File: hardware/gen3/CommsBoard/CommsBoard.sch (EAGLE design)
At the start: 41 parts, among them U1 ATMEGA165PV-8AU

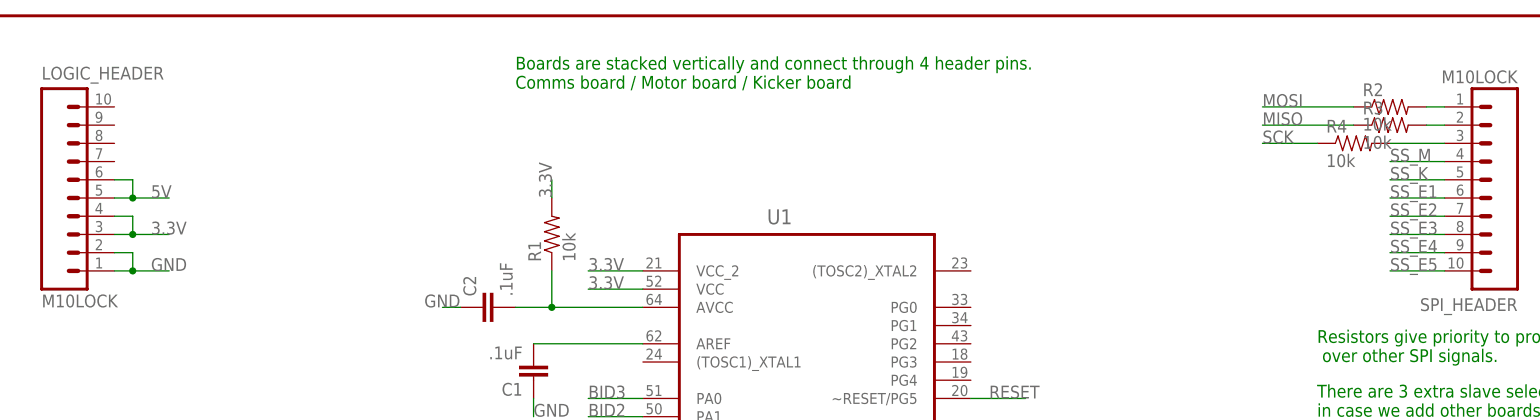
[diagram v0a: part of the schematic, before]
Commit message: some decoupling for power lines
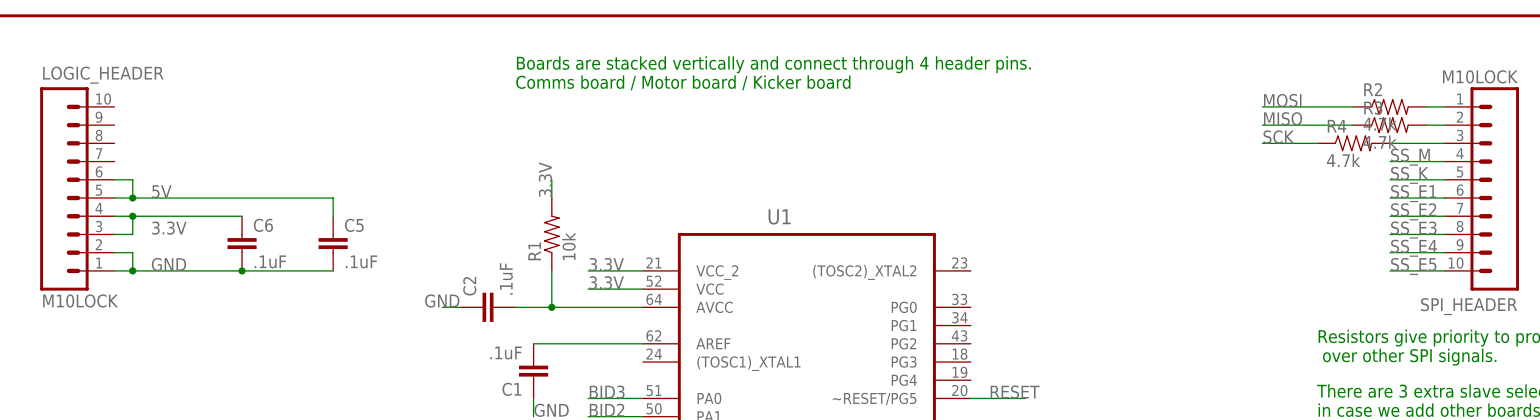
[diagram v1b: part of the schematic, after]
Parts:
- added C5, C6: .1uF, SparkFun-Capacitors:CAP0805
- R2, R3, R4: value 10k -> 4.7k
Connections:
- net 3.3V: now also C6.1
- net 5V: now also C5.1
- net GND: now also C5.2, C6.2
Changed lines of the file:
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@@
 <layers>
 <layer number="1" name="Top" color="4" fill="1" visible="no" active="no"/>
+<layer number="2" name="Route2" color="1" fill="3" visible="no" active="no"/>
+<layer number="3" name="Route3" color="4" fill="3" visible="no" active="no"/>
+<layer number="14" name="Route14" color="1" fill="6" visible="no" active="no"/>
+<layer number="15" name="Route15" color="4" fill="6" visible="no" active="no"/>
 <layer number="16" name="Bottom" color="1" fill="1" visible="no" active="no"/>
 <layer number="17" name="Pads" color="2" fill="1" visible="no" active="no"/>
@@
 <layer number="223" name="223bmp" color="24" fill="1" visible="no" active="no"/>
 <layer number="224" name="224bmp" color="25" fill="1" visible="no" active="no"/>
+<layer number="225" name="225bmp" color="7" fill="1" visible="yes" active="yes"/>
+<layer number="226" name="226bmp" color="7" fill="1" visible="yes" active="yes"/>
+<layer number="227" name="227bmp" color="7" fill="1" visible="yes" active="yes"/>
+<layer number="228" name="228bmp" color="7" fill="1" visible="yes" active="yes"/>
+<layer number="229" name="229bmp" color="7" fill="1" visible="yes" active="yes"/>
+<layer number="230" name="230bmp" color="7" fill="1" visible="yes" active="yes"/>
+<layer number="231" name="231bmp" color="7" fill="1" visible="yes" active="yes"/>
 <layer number="248" name="Housing" color="7" fill="1" visible="yes" active="yes"/>
 <layer number="249" name="Edge" color="7" fill="1" visible="yes" active="yes"/>
@@
 <part name="C2" library="SparkFun-Capacitors" deviceset="CAP" device="0805" value=".1uF"/>
 <part name="R1" library="SparkFun-Passives" deviceset="RESISTOR" device="0805-RES" value="10k"/>
-<part name="R2" library="SparkFun-Passives" deviceset="RESISTOR" device="0805-RES" value="10k"/>
-<part name="R3" library="SparkFun-Passives" deviceset="RESISTOR" device="0805-RES" value="10k"/>
-<part name="R4" library="SparkFun-Passives" deviceset="RESISTOR" device="0805-RES" value="10k"/>
+<part name="R2" library="SparkFun-Passives" deviceset="RESISTOR" device="0805-RES" value="4.7k"/>
+<part name="R3" library="SparkFun-Passives" deviceset="RESISTOR" device="0805-RES" value="4.7k"/>
+<part name="R4" library="SparkFun-Passives" deviceset="RESISTOR" device="0805-RES" value="4.7k"/>
 <part name="FRAME2" library="SparkFun-Aesthetics" deviceset="FRAME-LETTER" device=""/>
 <part name="ROBID" library="SparkFun-Electromechanical" deviceset="4-POS-DIP" device=""/>
@@
 <part name="U1" library="gen3" deviceset="ATMEGA165PV-8AU" device=""/>
 <part name="JP1" library="SparkFun-Connectors" deviceset="M05X2" device="PTH"/>
+<part name="C5" library="SparkFun-Capacitors" deviceset="CAP" device="0805" value=".1uF"/>
+<part name="C6" library="SparkFun-Capacitors" deviceset="CAP" device="0805" value=".1uF"/>
 </parts>
 <sheets>
@@
 <instance part="U1" gate="A" x="129.54" y="106.68"/>
 <instance part="JP1" gate="G$1" x="76.2" y="38.1"/>
+<instance part="C5" gate="G$1" x="63.5" y="152.4"/>
+<instance part="C6" gate="G$1" x="50.8" y="152.4"/>
 </instances>
 <busses>
@@
 <label x="38.1" y="149.86" size="1.778" layer="95"/>
 <pinref part="LOGIC_HEADER" gate="G$1" pin="2"/>
-<wire x1="35.56" y1="149.86" x2="40.64" y2="149.86" width="0.1524" layer="91"/>
 <wire x1="33.02" y1="152.4" x2="35.56" y2="152.4" width="0.1524" layer="91"/>
 <wire x1="35.56" y1="152.4" x2="35.56" y2="149.86" width="0.1524" layer="91"/>
@@
 <wire x1="35.56" y1="149.86" x2="33.02" y2="149.86" width="0.1524" layer="91"/>
 <junction x="35.56" y="149.86"/>
+<pinref part="C6" gate="G$1" pin="2"/>
+<wire x1="35.56" y1="149.86" x2="50.8" y2="149.86" width="0.1524" layer="91"/>
+<pinref part="C5" gate="G$1" pin="2"/>
+<wire x1="50.8" y1="149.86" x2="63.5" y2="149.86" width="0.1524" layer="91"/>
+<junction x="50.8" y="149.86"/>
 </segment>
 <segment>
@@
 <label x="38.1" y="154.94" size="1.778" layer="95"/>
 <pinref part="LOGIC_HEADER" gate="G$1" pin="4"/>
-<wire x1="35.56" y1="154.94" x2="40.64" y2="154.94" width="0.1524" layer="91"/>
 <wire x1="33.02" y1="157.48" x2="35.56" y2="157.48" width="0.1524" layer="91"/>
 <wire x1="35.56" y1="157.48" x2="35.56" y2="154.94" width="0.1524" layer="91"/>
-<junction x="35.56" y="154.94"/>
+<pinref part="C6" gate="G$1" pin="1"/>
+<wire x1="35.56" y1="157.48" x2="50.8" y2="157.48" width="0.1524" layer="91"/>
+<junction x="35.56" y="157.48"/>
 </segment>
 <segment>
@@
 <label x="38.1" y="160.02" size="1.778" layer="95"/>
 <pinref part="LOGIC_HEADER" gate="G$1" pin="6"/>
-<wire x1="35.56" y1="160.02" x2="40.64" y2="160.02" width="0.1524" layer="91"/>
 <wire x1="33.02" y1="162.56" x2="35.56" y2="162.56" width="0.1524" layer="91"/>
 <wire x1="35.56" y1="162.56" x2="35.56" y2="160.02" width="0.1524" layer="91"/>
 <junction x="35.56" y="160.02"/>
-</segment>
-</net>
+<pinref part="C5" gate="G$1" pin="1"/>
+<wire x1="35.56" y1="160.02" x2="63.5" y2="160.02" width="0.1524" layer="91"/>
+<wire x1="63.5" y1="160.02" x2="63.5" y2="157.48" width="0.1524" layer="91"/>
+</segment>
+</net>

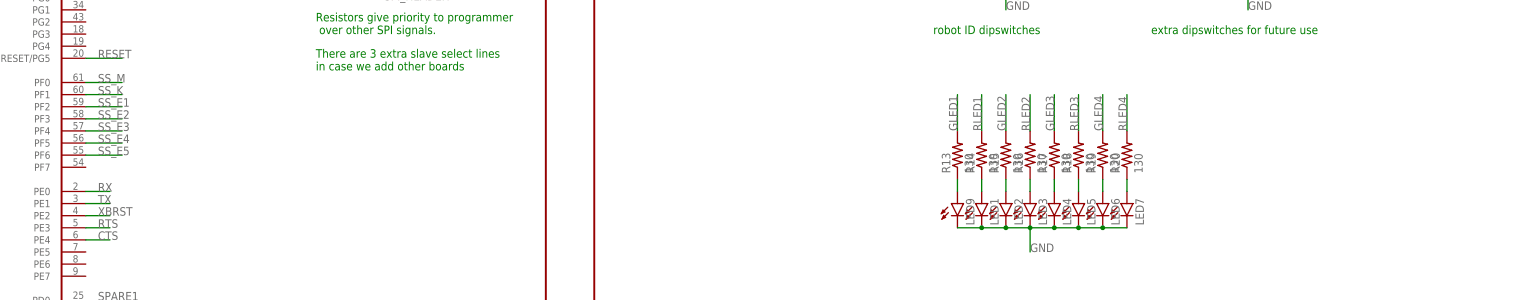
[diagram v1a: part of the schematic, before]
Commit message: added tmp sensor
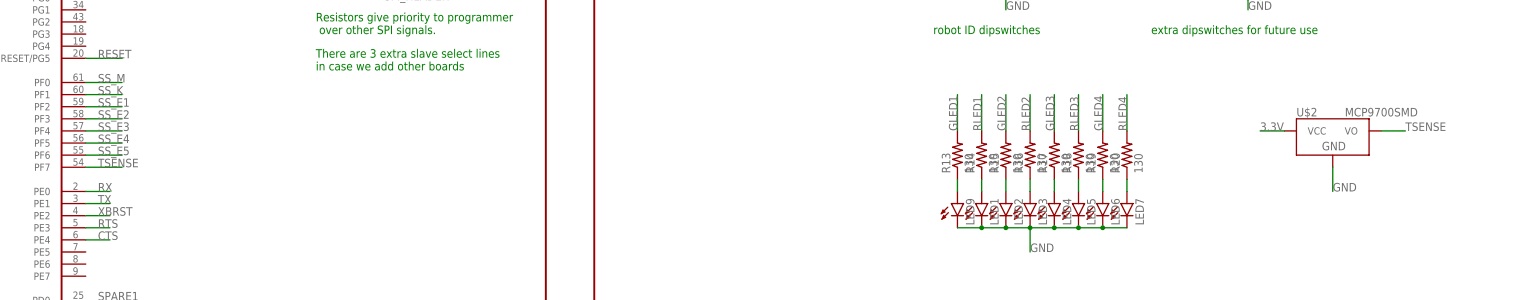
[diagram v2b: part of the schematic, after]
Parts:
- added U$2: MCP9700SMD, SparkFun-Sensors:MCP9700SMD
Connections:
- new net TSENSE: U$2.VO, U1.PF7
- net 3.3V: now also U$2.VCC
- net GND: now also U$2.GND
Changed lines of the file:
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@@
 <part name="C5" library="SparkFun-Capacitors" deviceset="CAP" device="0805" value=".1uF"/>
 <part name="C6" library="SparkFun-Capacitors" deviceset="CAP" device="0805" value=".1uF"/>
+<part name="U$2" library="SparkFun-Sensors" deviceset="MCP9700" device="SMD"/>
 </parts>
 <sheets>
@@
 <instance part="C5" gate="G$1" x="63.5" y="152.4"/>
 <instance part="C6" gate="G$1" x="50.8" y="152.4"/>
+<instance part="U$2" gate="G$1" x="414.02" y="114.3"/>
 </instances>
 <busses>
@@
 <label x="86.36" y="33.02" size="1.778" layer="95"/>
 </segment>
+<segment>
+<pinref part="U$2" gate="G$1" pin="GND"/>
+<wire x1="414.02" y1="109.22" x2="414.02" y2="104.14" width="0.1524" layer="91"/>
+<label x="414.02" y="104.14" size="1.778" layer="95"/>
+</segment>
 </net>
 <net name="3.3V" class="0">
@@
 <wire x1="83.82" y1="43.18" x2="88.9" y2="43.18" width="0.1524" layer="91"/>
 <label x="86.36" y="43.18" size="1.778" layer="95"/>
+</segment>
+<segment>
+<pinref part="U$2" gate="G$1" pin="VCC"/>
+<wire x1="403.86" y1="116.84" x2="398.78" y2="116.84" width="0.1524" layer="91"/>
+<label x="398.78" y="116.84" size="1.778" layer="95"/>
 </segment>
 </net>
@@
 </segment>
 </net>
+<net name="TSENSE" class="0">
+<segment>
+<pinref part="U$2" gate="G$1" pin="VO"/>
+<wire x1="424.18" y1="116.84" x2="429.26" y2="116.84" width="0.1524" layer="91"/>
+<label x="429.26" y="116.84" size="1.778" layer="95"/>
+</segment>
+<segment>
+<pinref part="U1" gate="A" pin="PF7"/>
+<wire x1="152.4" y1="109.22" x2="160.02" y2="109.22" width="0.1524" layer="91"/>
+<label x="154.94" y="109.22" size="1.778" layer="95"/>
+</segment>
+</net>

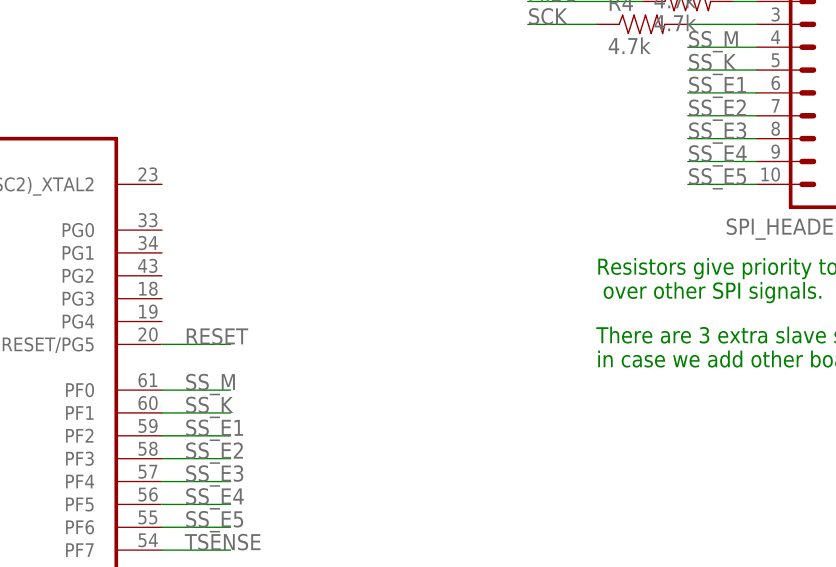
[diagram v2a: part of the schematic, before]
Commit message: Added reset button to comms
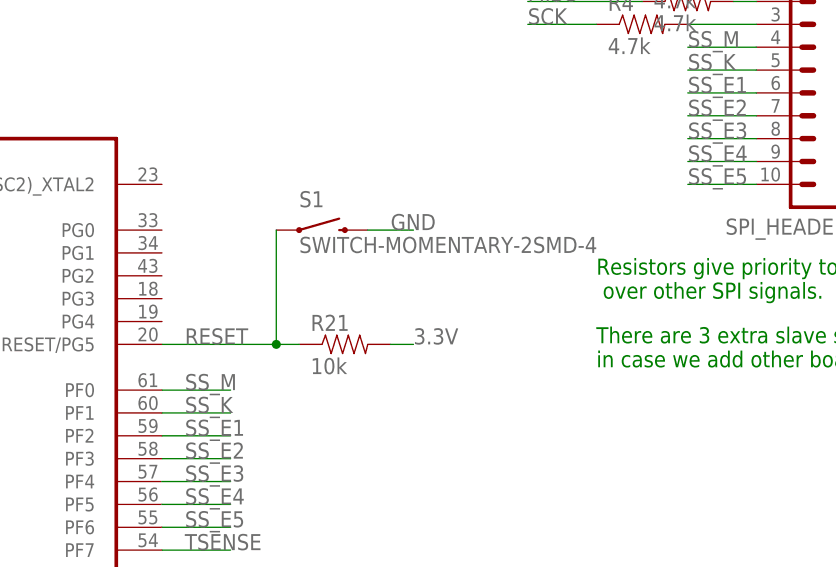
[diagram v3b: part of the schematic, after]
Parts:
- added R21: 10k, SparkFun-Passives:RESISTOR0805-RES
- added S1: SWITCH-MOMENTARY-2SMD-4, SparkFun-Electromechanical:SWITCH-MOMENTARY-2SMD-4
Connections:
- net 3.3V: now also R21.2
- net GND: now also S1.2
- net RESET: now also R21.1, S1.1
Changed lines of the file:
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@@
 <?xml version="1.0" encoding="utf-8"?>
 <!DOCTYPE eagle SYSTEM "eagle.dtd">
-<eagle version="6.4">
+<eagle version="7.2.0">
 <drawing>
 <settings>
@@
 <part name="C6" library="SparkFun-Capacitors" deviceset="CAP" device="0805" value=".1uF"/>
 <part name="U$2" library="SparkFun-Sensors" deviceset="MCP9700" device="SMD"/>
+<part name="S1" library="SparkFun-Electromechanical" deviceset="SWITCH-MOMENTARY-2" device="SMD-4"/>
+<part name="R21" library="SparkFun-Passives" deviceset="RESISTOR" device="0805-RES" value="10k"/>
 </parts>
 <sheets>
@@
 <instance part="C6" gate="G$1" x="50.8" y="152.4"/>
 <instance part="U$2" gate="G$1" x="414.02" y="114.3"/>
+<instance part="S1" gate="G$1" x="170.18" y="144.78"/>
+<instance part="R21" gate="G$1" x="172.72" y="132.08"/>
 </instances>
 <busses>
@@
 <label x="414.02" y="104.14" size="1.778" layer="95"/>
 </segment>
+<segment>
+<pinref part="S1" gate="G$1" pin="2"/>
+<wire x1="175.26" y1="144.78" x2="180.34" y2="144.78" width="0.1524" layer="91"/>
+<label x="177.8" y="144.78" size="1.778" layer="95"/>
+</segment>
 </net>
 <net name="3.3V" class="0">
@@
 <label x="398.78" y="116.84" size="1.778" layer="95"/>
 </segment>
+<segment>
+<pinref part="R21" gate="G$1" pin="2"/>
+<wire x1="177.8" y1="132.08" x2="180.34" y2="132.08" width="0.1524" layer="91"/>
+<label x="180.34" y="132.08" size="1.778" layer="95"/>
+</segment>
 </net>
 <net name="FILT" class="0">
@@
 <net name="RESET" class="0">
 <segment>
-<wire x1="152.4" y1="132.08" x2="160.02" y2="132.08" width="0.1524" layer="91"/>
+<wire x1="152.4" y1="132.08" x2="165.1" y2="132.08" width="0.1524" layer="91"/>
 <label x="154.94" y="132.08" size="1.778" layer="95"/>
 <pinref part="U1" gate="A" pin="~RESET/PG5"/>
-</segment>
-<segment>
+<pinref part="S1" gate="G$1" pin="1"/>
+<wire x1="165.1" y1="132.08" x2="165.1" y2="144.78" width="0.1524" layer="91"/>
+<pinref part="R21" gate="G$1" pin="1"/>
+<wire x1="165.1" y1="132.08" x2="167.64" y2="132.08" width="0.1524" layer="91"/>
+<junction x="165.1" y="132.08"/>
+</segment>
+<segment>

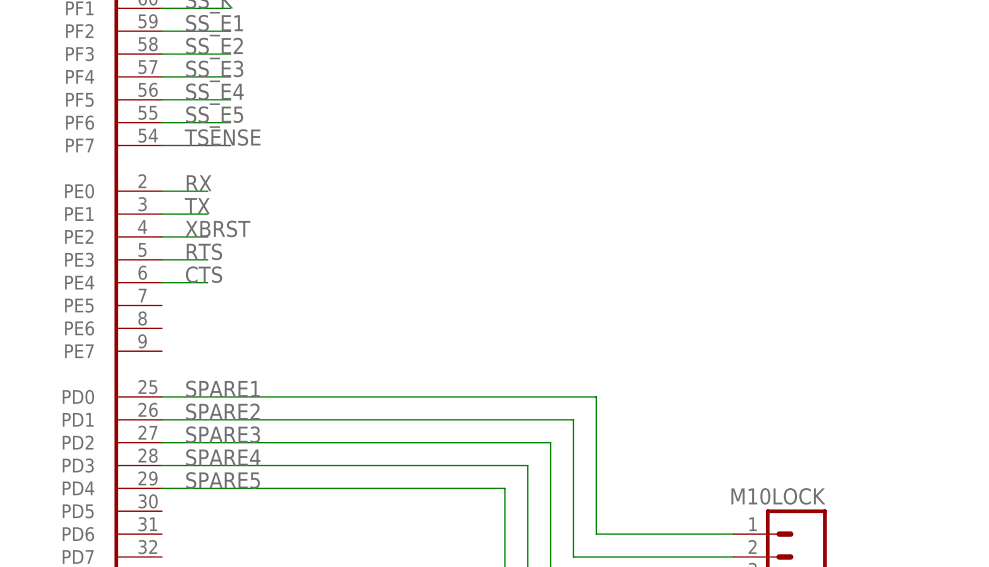
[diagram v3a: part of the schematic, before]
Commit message: Added IMU header to comms board
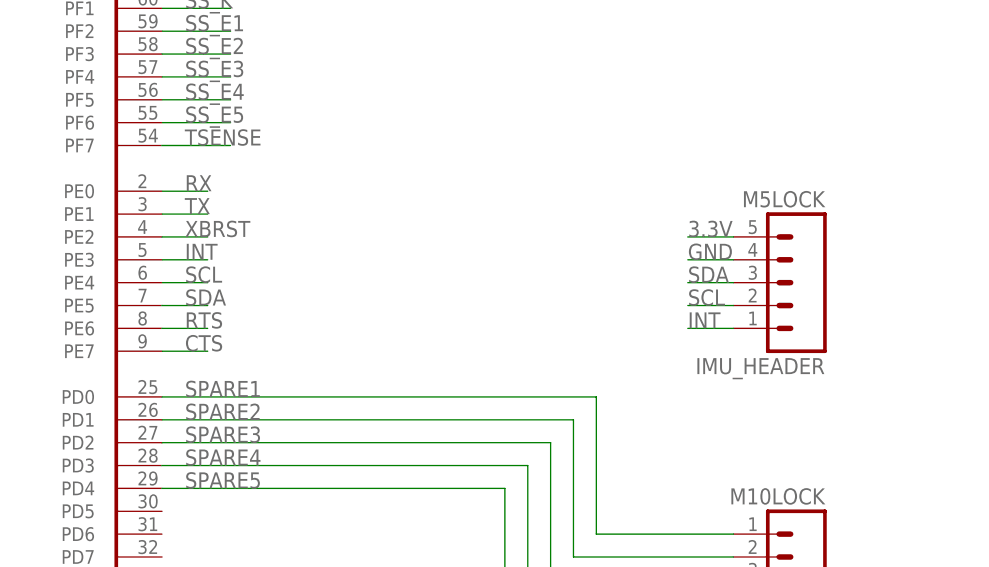
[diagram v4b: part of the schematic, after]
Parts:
- added M5LOCK: IMU_HEADER, SparkFun-Connectors:M05LOCK
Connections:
- new net INT: M5LOCK.1, U1.PE3
- new net SCL: M5LOCK.2, U1.PE4
- new net SDA: M5LOCK.3, U1.PE5
- net 3.3V: now also M5LOCK.5
- net CTS: now also U1.PE7; no longer U1.PE4
- net GND: now also M5LOCK.4
- net RTS: now also U1.PE6; no longer U1.PE3
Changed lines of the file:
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@@
 <part name="S1" library="SparkFun-Electromechanical" deviceset="SWITCH-MOMENTARY-2" device="SMD-4"/>
 <part name="R21" library="SparkFun-Passives" deviceset="RESISTOR" device="0805-RES" value="10k"/>
+<part name="M5LOCK" library="SparkFun-Connectors" deviceset="M05" device="LOCK" value="IMU_HEADER"/>
 </parts>
 <sheets>
@@
 <instance part="S1" gate="G$1" x="170.18" y="144.78"/>
 <instance part="R21" gate="G$1" x="172.72" y="132.08"/>
+<instance part="M5LOCK" gate="G$1" x="223.52" y="93.98" rot="MR0"/>
 </instances>
 <busses>
@@
 <label x="177.8" y="144.78" size="1.778" layer="95"/>
 </segment>
+<segment>
+<pinref part="M5LOCK" gate="G$1" pin="4"/>
+<wire x1="215.9" y1="96.52" x2="210.82" y2="96.52" width="0.1524" layer="91"/>
+<label x="210.82" y="96.52" size="1.778" layer="95"/>
+</segment>
 </net>
 <net name="3.3V" class="0">
@@
 <wire x1="177.8" y1="132.08" x2="180.34" y2="132.08" width="0.1524" layer="91"/>
 <label x="180.34" y="132.08" size="1.778" layer="95"/>
+</segment>
+<segment>
+<pinref part="M5LOCK" gate="G$1" pin="5"/>
+<wire x1="215.9" y1="99.06" x2="210.82" y2="99.06" width="0.1524" layer="91"/>
+<label x="210.82" y="99.06" size="1.778" layer="95"/>
 </segment>
 </net>
@@
 </segment>
 <segment>
-<pinref part="U1" gate="A" pin="PE3"/>
-<wire x1="152.4" y1="96.52" x2="157.48" y2="96.52" width="0.1524" layer="91"/>
-<label x="154.94" y="96.52" size="1.778" layer="95"/>
+<pinref part="U1" gate="A" pin="PE6"/>
+<wire x1="152.4" y1="88.9" x2="157.48" y2="88.9" width="0.1524" layer="91"/>
+<label x="154.94" y="88.9" size="1.778" layer="95"/>
 </segment>
 </net>
@@
 </segment>
 <segment>
-<pinref part="U1" gate="A" pin="PE4"/>
-<wire x1="152.4" y1="93.98" x2="157.48" y2="93.98" width="0.1524" layer="91"/>
-<label x="154.94" y="93.98" size="1.778" layer="95"/>
+<pinref part="U1" gate="A" pin="PE7"/>
+<wire x1="152.4" y1="86.36" x2="157.48" y2="86.36" width="0.1524" layer="91"/>
+<label x="154.94" y="86.36" size="1.778" layer="95"/>
 </segment>
 </net>
@@
 </segment>
 </net>
+<net name="INT" class="0">
+<segment>
+<pinref part="U1" gate="A" pin="PE3"/>
+<wire x1="152.4" y1="96.52" x2="157.48" y2="96.52" width="0.1524" layer="91"/>
+<label x="154.94" y="96.52" size="1.778" layer="95"/>
+</segment>
+<segment>
+<pinref part="M5LOCK" gate="G$1" pin="1"/>
+<wire x1="215.9" y1="88.9" x2="210.82" y2="88.9" width="0.1524" layer="91"/>
+<label x="210.82" y="88.9" size="1.778" layer="95"/>
+</segment>
+</net>
+<net name="SCL" class="0">
+<segment>
+<pinref part="U1" gate="A" pin="PE4"/>
+<wire x1="152.4" y1="93.98" x2="157.48" y2="93.98" width="0.1524" layer="91"/>
+<label x="154.94" y="93.98" size="1.778" layer="95"/>
+</segment>
+<segment>
+<pinref part="M5LOCK" gate="G$1" pin="2"/>
+<wire x1="215.9" y1="91.44" x2="210.82" y2="91.44" width="0.1524" layer="91"/>
+<label x="210.82" y="91.44" size="1.778" layer="95"/>
+</segment>
+</net>
+<net name="SDA" class="0">
+<segment>
+<pinref part="U1" gate="A" pin="PE5"/>
+<wire x1="152.4" y1="91.44" x2="157.48" y2="91.44" width="0.1524" layer="91"/>
+<label x="154.94" y="91.44" size="1.778" layer="95"/>
+</segment>
+<segment>
+<pinref part="M5LOCK" gate="G$1" pin="3"/>
+<wire x1="215.9" y1="93.98" x2="210.82" y2="93.98" width="0.1524" layer="91"/>
+<label x="210.82" y="93.98" size="1.778" layer="95"/>
+</segment>
+</net>
